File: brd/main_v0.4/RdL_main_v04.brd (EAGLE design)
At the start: 56.7 x 30.2 mm, 39 parts, among them J1 Test, J3 GND, J4 GND, U1 MPU-6000QFN-24

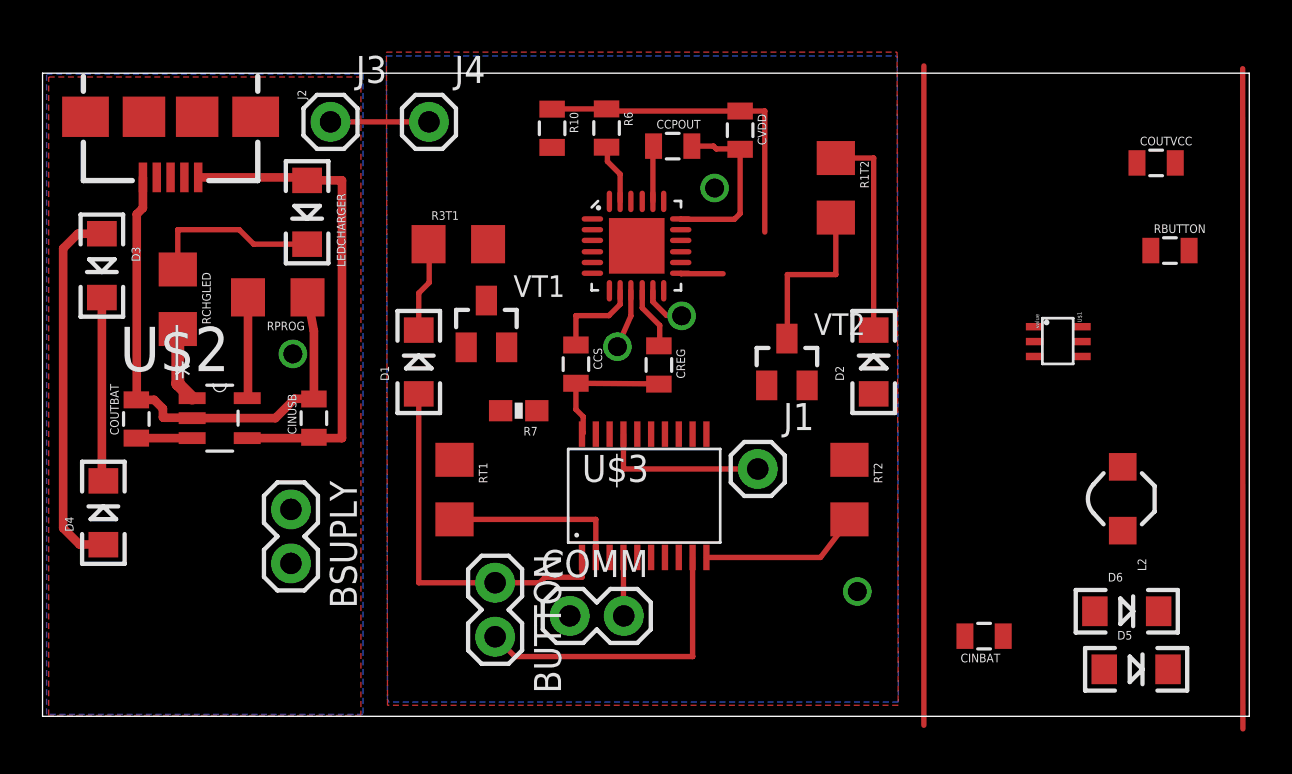
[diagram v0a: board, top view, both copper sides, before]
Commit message: Update main v4, almost ready for printing
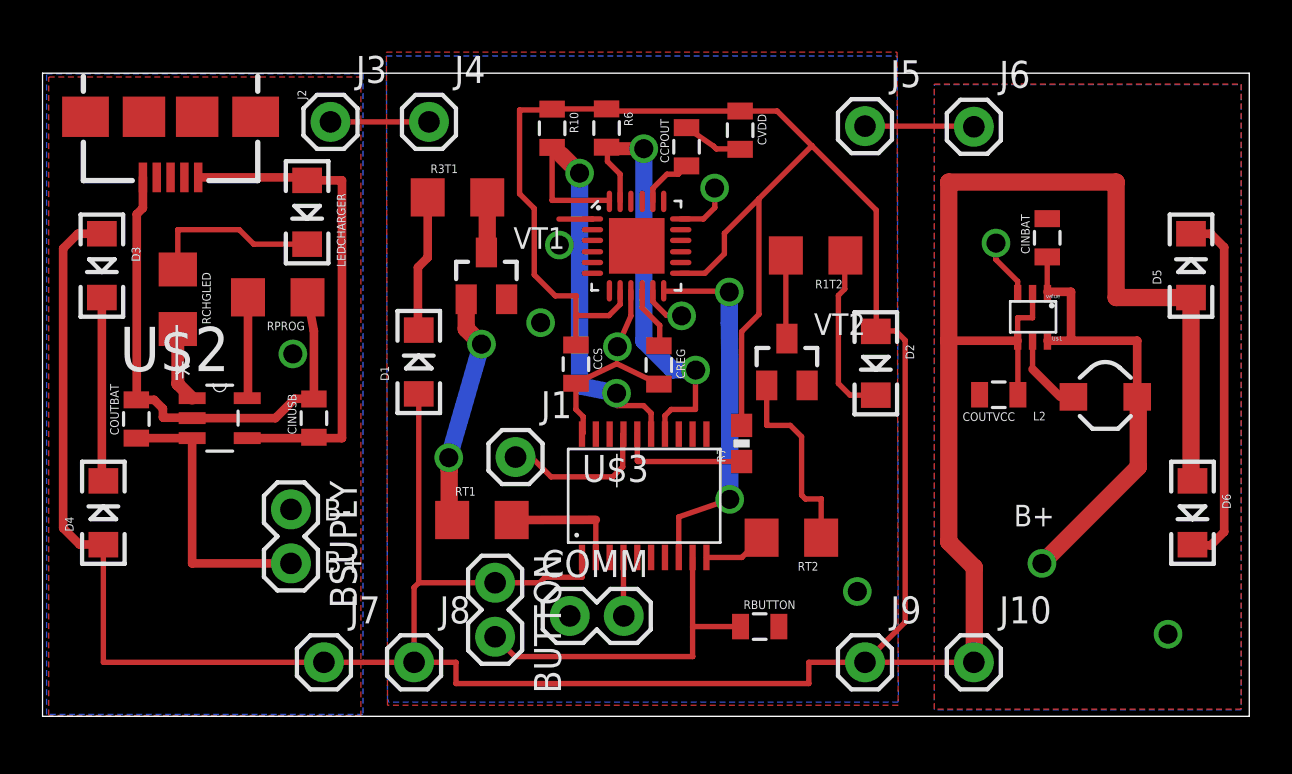
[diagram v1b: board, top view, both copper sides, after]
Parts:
- added J10, J7, J8, J9: VCC, SparkFun-Connectors:1X01
- added J5, J6: GND, SparkFun-Connectors:1X01
- moved RBUTTON 26.2 mm to (33.7, 4.22)
- moved D5 19.2 mm to (54.0, 21.2), turned to 90 degrees
- moved CINBAT 19.0 mm to (47.2, 22.5), turned to 90 degrees
- moved COUTVCC 13.2 mm to (45.0, 15.1), turned to 180 degrees
- moved J1 11.4 mm to (22.2, 12.2)
- moved R7 10.6 mm to (32.9, 12.8), turned to 90 degrees
- moved D6 5.57 mm to (54.1, 9.57), turned to 270 degrees
- moved U$1 5.14 mm to (44.2, 19.9), turned to 180 degrees
- moved L2 4.86 mm to (50.0, 15.0), turned to 180 degrees
- moved RT2 3.54 mm to (35.2, 8.40), turned to 180 degrees
- moved R1T2 3.32 mm to (36.4, 21.7), turned to 180 degrees
- moved VT1 2.26 mm to (20.9, 20.7)
- moved R3T1 2.20 mm to (19.5, 24.4)
- moved RT1 1.93 mm to (20.7, 9.23), turned to 0 degrees
- moved CCPOUT 0.65 mm to (30.3, 26.8), turned to 90 degrees
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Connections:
- net GND: now also J5.1, J6.1
- net VCC: now also J10.1, J7.1, J8.1, J9.1
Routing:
- net VCC: track 57.3 -> 222.6 mm
- net VOUTBATT: track 2.62 -> 35.0 mm, vias 0 -> 1
- net N$25: track 31.0 -> 0.00 mm
- net N$24: track 31.0 -> 0.00 mm
- net N$20: track 0.00 -> 22.1 mm, vias 0 -> 2
- net N$22: track 2.81 -> 20.9 mm, vias 0 -> 2
- net N$18: track 0.00 -> 17.4 mm, vias 0 -> 2
- net N$13: track 9.87 -> 25.1 mm
- net N$8: track 0.00 -> 10.9 mm, vias 0 -> 2
- net N$9: track 0.00 -> 9.32 mm
- net GND: track 48.9 -> 56.3 mm, vias 5 -> 9
- net N$12: track 0.00 -> 6.17 mm
- net N$11: track 7.61 -> 2.98 mm
- net N$6: track 7.99 -> 3.93 mm
- net N$3: track 0.00 -> 3.80 mm
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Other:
- board text added: "B+"
- board text added: "B-"

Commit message: Version 4 without unrouted vias
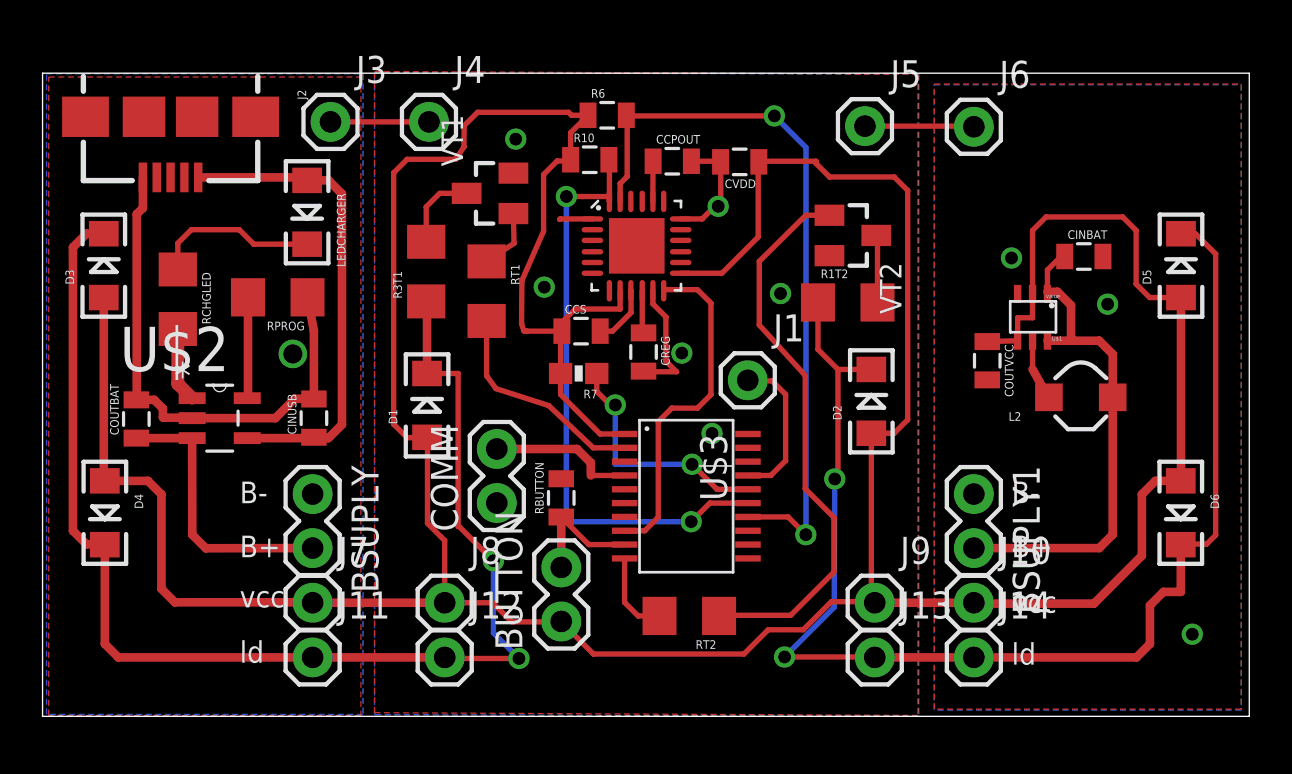
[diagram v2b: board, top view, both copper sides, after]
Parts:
- added BSUPLY1: In, SparkFun-Connectors:1X02
- added J11, J12, J13, J14: LEDS1, SparkFun-Connectors:1X01
- moved J1 11.5 mm to (33.2, 15.8)
- moved RBUTTON 11.1 mm to (24.4, 10.3), turned to 90 degrees
- moved RT1 10.8 mm to (20.9, 20.0), turned to 270 degrees
- moved R7 8.34 mm to (25.2, 16.1), turned to 180 degrees
- moved VT2 6.71 mm to (38.1, 22.6), turned to 270 degrees
- moved COMM 6.32 mm to (21.4, 10.0), turned to 90 degrees
- moved RT2 6.05 mm to (30.4, 4.72)
- moved VT1 3.88 mm to (21.0, 24.6), turned to 90 degrees
- moved R3T1 3.79 mm to (18.0, 20.9), turned to 90 degrees
- moved BUTTON 3.60 mm to (24.4, 4.46), turned to 90 degrees
- moved J8 3.15 mm to (18.9, 5.34)
- moved J7 2.85 mm to (12.7, 5.34)
- moved J9 2.84 mm to (39.1, 5.34)
- moved J10 2.80 mm to (43.8, 5.34)
- moved R1T2 2.68 mm to (37.9, 19.5), turned to 0 degrees
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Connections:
- net GND: now also BSUPLY1.1
- net N$13: now also J13.1, J14.1
- net N$14: now also J11.1, J12.1
- net VOUTBATT: now also BSUPLY1.2
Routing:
- net N$14: track 15.1 -> 60.7 mm, vias 0 -> 2
- net N$13: track 25.1 -> 59.9 mm, vias 0 -> 2
- net VCC: track 222.6 -> 189.3 mm
- net N$9: track 9.32 -> 26.5 mm
- net N$22: track 20.9 -> 34.5 mm
- net N$1: track 16.6 -> 5.89 mm
- net N$8: track 10.9 -> 2.95 mm, vias 2 -> 0
- net N$20: track 22.1 -> 28.4 mm
- net GND: track 56.3 -> 50.2 mm, vias 9 -> 10
- net N$12: track 6.17 -> 11.5 mm, vias 0 -> 2
- net N$10: track 5.73 -> 10.3 mm
- net N$15: track 2.76 -> 6.87 mm
- net VOUTBATT: track 35.0 -> 37.0 mm, vias 1 -> 0
- net N$7: track 2.61 -> 3.81 mm
- net N$18: track 17.4 -> 16.2 mm, vias 2 -> 0
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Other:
- board text added: "ld"
- board text added: "vcc"
